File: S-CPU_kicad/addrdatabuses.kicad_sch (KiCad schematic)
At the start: 179 parts

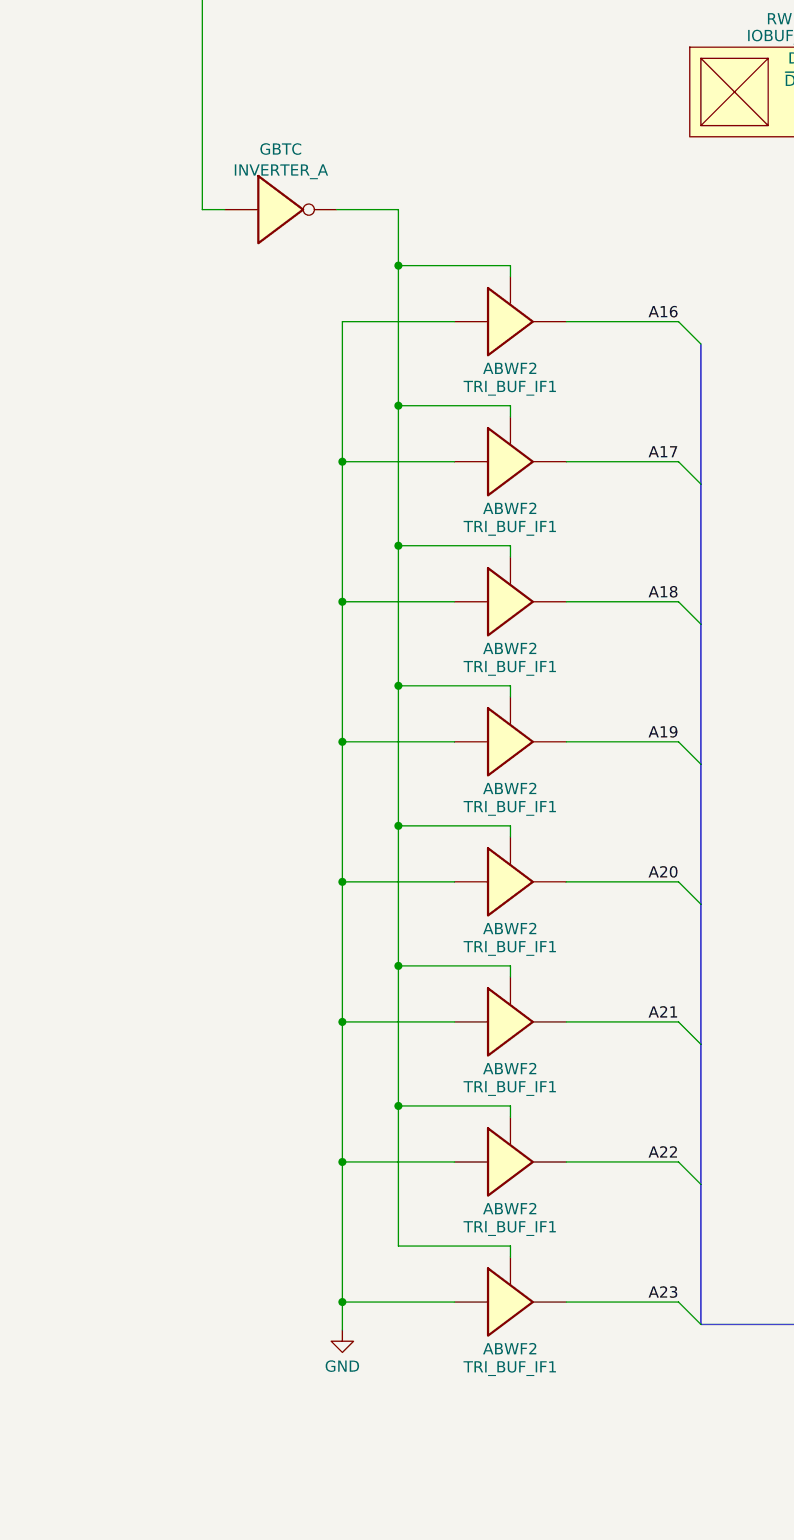
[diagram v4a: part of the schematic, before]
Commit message: Some cells had the wrong ID in the producter remainder sheet. Allocation of new names in spreadsheet for cells in the DMA section
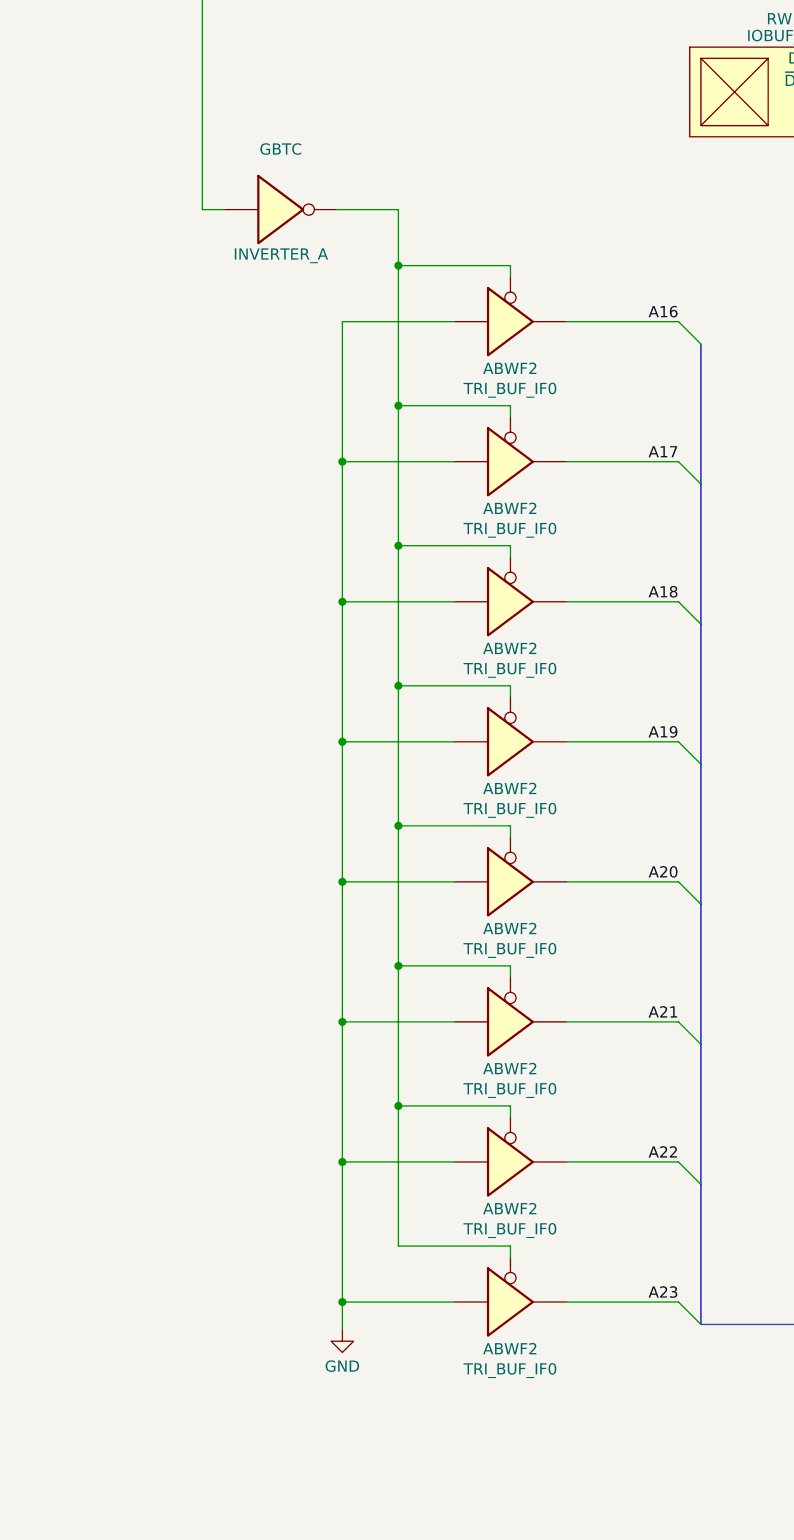
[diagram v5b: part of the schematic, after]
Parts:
- ABWF2: value TRI_BUF_IF1 -> TRI_BUF_IF0; symbol Ricoh_Cells:TRI_BUF_IF1 -> Ricoh_Cells:TRI_BUF_IF0
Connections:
- net A16: now also ABWF2.4; no longer ABWF2.4
- net A17: now also ABWF2.4; no longer ABWF2.4
- net A18: now also ABWF2.4; no longer ABWF2.4
- net A19: now also ABWF2.4; no longer ABWF2.4
- net A20: now also ABWF2.4; no longer ABWF2.4
- net A21: now also ABWF2.4; no longer ABWF2.4
- net A22: now also ABWF2.4; no longer ABWF2.4
- net A23: now also ABWF2.4; no longer ABWF2.4
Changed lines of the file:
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@@
     )
   )
-  (symbol (lib_id "Ricoh_Cells:TRI_BUF_IF1") (at 103.505 212.725 0) (unit 1)
+  (symbol (lib_id "Ricoh_Cells:TRI_BUF_IF0") (at 103.505 133.35 0) (unit 1)
     (in_bom yes) (on_board yes) (dnp no) (fields_autoplaced)
-    (property "Reference" "ABWF2" (at 103.505 218.067 0)
+    (property "Reference" "ABWF2" (at 103.505 138.692 0)
       (effects (font (size 1.27 1.27)))
     )
-    (property "Value" "TRI_BUF_IF1" (at 103.505 220.115 0)
+    (property "Value" "TRI_BUF_IF0" (at 103.505 140.97 0)
       (effects (font (size 1.27 1.27)))
     )
-    (property "Footprint" "" (at 100.965 212.725 0)
+    (property "Footprint" "" (at 100.965 133.35 0)
       (effects (font (size 1.27 1.27)) hide)
     )
-    (property "Datasheet" "http://iceboy.a-singer.de/doc/dmg_cells.html#tri_inv_if0" (at 104.775 222.885 0)
+    (property "Datasheet" "http://iceboy.a-singer.de/doc/dmg_cells.html#tri_buf_if0" (at 104.775 143.51 0)
       (effects (font (size 1.27 1.27)) hide)
     )
@@
     )
   )
-  (symbol (lib_id "Ricoh_Cells:TRI_BUF_IF1") (at 103.505 133.35 0) (unit 1)
+  (symbol (lib_id "Ricoh_Cells:TRI_BUF_IF0") (at 103.505 212.725 0) (unit 1)
     (in_bom yes) (on_board yes) (dnp no) (fields_autoplaced)
-    (property "Reference" "ABWF2" (at 103.505 138.692 0)
+    (property "Reference" "ABWF2" (at 103.505 218.067 0)
       (effects (font (size 1.27 1.27)))
     )
-    (property "Value" "TRI_BUF_IF1" (at 103.505 140.74 0)
+    (property "Value" "TRI_BUF_IF0" (at 103.505 220.345 0)
       (effects (font (size 1.27 1.27)))
     )
-    (property "Footprint" "" (at 100.965 133.35 0)
+    (property "Footprint" "" (at 100.965 212.725 0)
       (effects (font (size 1.27 1.27)) hide)
     )
-    (property "Datasheet" "http://iceboy.a-singer.de/doc/dmg_cells.html#tri_inv_if0" (at 104.775 143.51 0)
+    (property "Datasheet" "http://iceboy.a-singer.de/doc/dmg_cells.html#tri_buf_if0" (at 104.775 222.885 0)
       (effects (font (size 1.27 1.27)) hide)
     )
@@
     )
   )
-  (symbol (lib_id "Ricoh_Cells:TRI_BUF_IF1") (at 103.505 196.85 0) (unit 1)
+  (symbol (lib_id "Ricoh_Cells:TRI_BUF_IF0") (at 103.505 149.225 0) (unit 1)
     (in_bom yes) (on_board yes) (dnp no) (fields_autoplaced)
-    (property "Reference" "ABWF2" (at 103.505 202.192 0)
+    (property "Reference" "ABWF2" (at 103.505 154.567 0)
       (effects (font (size 1.27 1.27)))
     )
-    (property "Value" "TRI_BUF_IF1" (at 103.505 204.24 0)
+    (property "Value" "TRI_BUF_IF0" (at 103.505 156.845 0)
       (effects (font (size 1.27 1.27)))
     )
-    (property "Footprint" "" (at 100.965 196.85 0)
+    (property "Footprint" "" (at 100.965 149.225 0)
       (effects (font (size 1.27 1.27)) hide)
     )
-    (property "Datasheet" "http://iceboy.a-singer.de/doc/dmg_cells.html#tri_inv_if0" (at 104.775 207.01 0)
+    (property "Datasheet" "http://iceboy.a-singer.de/doc/dmg_cells.html#tri_buf_if0" (at 104.775 159.385 0)
       (effects (font (size 1.27 1.27)) hide)
     )
@@
     )
   )
-  (symbol (lib_id "Ricoh_Cells:TRI_BUF_IF1") (at 103.505 228.6 0) (unit 1)
+  (symbol (lib_id "Ricoh_Cells:TRI_BUF_IF0") (at 103.505 117.475 0) (unit 1)
     (in_bom yes) (on_board yes) (dnp no) (fields_autoplaced)
-    (property "Reference" "ABWF2" (at 103.505 233.942 0)
+    (property "Reference" "ABWF2" (at 103.505 122.817 0)
       (effects (font (size 1.27 1.27)))
     )
-    (property "Value" "TRI_BUF_IF1" (at 103.505 235.99 0)
+    (property "Value" "TRI_BUF_IF0" (at 103.505 125.095 0)
       (effects (font (size 1.27 1.27)))
     )
-    (property "Footprint" "" (at 100.965 228.6 0)
+    (property "Footprint" "" (at 100.965 117.475 0)
       (effects (font (size 1.27 1.27)) hide)
     )
-    (property "Datasheet" "http://iceboy.a-singer.de/doc/dmg_cells.html#tri_inv_if0" (at 104.775 238.76 0)
+    (property "Datasheet" "http://iceboy.a-singer.de/doc/dmg_cells.html#tri_buf_if0" (at 104.775 127.635 0)
       (effects (font (size 1.27 1.27)) hide)
     )
@@
     )
   )
-  (symbol (lib_id "Ricoh_Cells:TRI_BUF_IF1") (at 103.505 180.975 0) (unit 1)
+  (symbol (lib_id "Ricoh_Cells:TRI_BUF_IF0") (at 103.505 165.1 0) (unit 1)
     (in_bom yes) (on_board yes) (dnp no) (fields_autoplaced)
-    (property "Reference" "ABWF2" (at 103.505 186.317 0)
+    (property "Reference" "ABWF2" (at 103.505 170.442 0)
       (effects (font (size 1.27 1.27)))
     )
-    (property "Value" "TRI_BUF_IF1" (at 103.505 188.365 0)
+    (property "Value" "TRI_BUF_IF0" (at 103.505 172.72 0)
       (effects (font (size 1.27 1.27)))
     )
-    (property "Footprint" "" (at 100.965 180.975 0)
+    (property "Footprint" "" (at 100.965 165.1 0)
       (effects (font (size 1.27 1.27)) hide)
     )
-    (property "Datasheet" "http://iceboy.a-singer.de/doc/dmg_cells.html#tri_inv_if0" (at 104.775 191.135 0)
+    (property "Datasheet" "http://iceboy.a-singer.de/doc/dmg_cells.html#tri_buf_if0" (at 104.775 175.26 0)
       (effects (font (size 1.27 1.27)) hide)
     )
@@
     )
   )
-  (symbol (lib_id "Ricoh_Cells:TRI_BUF_IF1") (at 103.505 117.475 0) (unit 1)
+  (symbol (lib_id "Ricoh_Cells:TRI_BUF_IF0") (at 103.505 228.6 0) (unit 1)
     (in_bom yes) (on_board yes) (dnp no) (fields_autoplaced)
-    (property "Reference" "ABWF2" (at 103.505 122.817 0)
+    (property "Reference" "ABWF2" (at 103.505 233.942 0)
       (effects (font (size 1.27 1.27)))
     )
-    (property "Value" "TRI_BUF_IF1" (at 103.505 124.865 0)
+    (property "Value" "TRI_BUF_IF0" (at 103.505 236.22 0)
       (effects (font (size 1.27 1.27)))
     )
-    (property "Footprint" "" (at 100.965 117.475 0)
+    (property "Footprint" "" (at 100.965 228.6 0)
       (effects (font (size 1.27 1.27)) hide)
     )
-    (property "Datasheet" "http://iceboy.a-singer.de/doc/dmg_cells.html#tri_inv_if0" (at 104.775 127.635 0)
+    (property "Datasheet" "http://iceboy.a-singer.de/doc/dmg_cells.html#tri_buf_if0" (at 104.775 238.76 0)
       (effects (font (size 1.27 1.27)) hide)
     )
@@
     )
   )
-  (symbol (lib_id "Ricoh_Cells:TRI_BUF_IF1") (at 103.505 165.1 0) (unit 1)
+  (symbol (lib_id "Ricoh_Cells:TRI_BUF_IF0") (at 103.505 180.975 0) (unit 1)
     (in_bom yes) (on_board yes) (dnp no) (fields_autoplaced)
-    (property "Reference" "ABWF2" (at 103.505 170.442 0)
+    (property "Reference" "ABWF2" (at 103.505 186.317 0)
       (effects (font (size 1.27 1.27)))
     )
-    (property "Value" "TRI_BUF_IF1" (at 103.505 172.49 0)
+    (property "Value" "TRI_BUF_IF0" (at 103.505 188.595 0)
       (effects (font (size 1.27 1.27)))
     )
-    (property "Footprint" "" (at 100.965 165.1 0)
+    (property "Footprint" "" (at 100.965 180.975 0)
       (effects (font (size 1.27 1.27)) hide)
     )
-    (property "Datasheet" "http://iceboy.a-singer.de/doc/dmg_cells.html#tri_inv_if0" (at 104.775 175.26 0)
+    (property "Datasheet" "http://iceboy.a-singer.de/doc/dmg_cells.html#tri_buf_if0" (at 104.775 191.135 0)
       (effects (font (size 1.27 1.27)) hide)
     )
@@
     )
   )
-  (symbol (lib_id "Ricoh_Cells:TRI_BUF_IF1") (at 103.505 149.225 0) (unit 1)
+  (symbol (lib_id "Ricoh_Cells:TRI_BUF_IF0") (at 103.505 196.85 0) (unit 1)
     (in_bom yes) (on_board yes) (dnp no) (fields_autoplaced)
-    (property "Reference" "ABWF2" (at 103.505 154.567 0)
+    (property "Reference" "ABWF2" (at 103.505 202.192 0)
       (effects (font (size 1.27 1.27)))
     )
-    (property "Value" "TRI_BUF_IF1" (at 103.505 156.615 0)
+    (property "Value" "TRI_BUF_IF0" (at 103.505 204.47 0)
       (effects (font (size 1.27 1.27)))
     )
-    (property "Footprint" "" (at 100.965 149.225 0)
+    (property "Footprint" "" (at 100.965 196.85 0)
       (effects (font (size 1.27 1.27)) hide)
     )
-    (property "Datasheet" "http://iceboy.a-singer.de/doc/dmg_cells.html#tri_inv_if0" (at 104.775 159.385 0)
+    (property "Datasheet" "http://iceboy.a-singer.de/doc/dmg_cells.html#tri_buf_if0" (at 104.775 207.01 0)
       (effects (font (size 1.27 1.27)) hide)
     )
@@
       (effects (font (size 1.27 1.27)))
     )
-    (property "Value" "INVERTER_A" (at 77.47 100.33 0)
+    (property "Value" "INVERTER_A" (at 77.47 109.855 0)
       (effects (font (size 1.27 1.27)))
     )
@@
         )
         (path "/ca9d3ca9-0297-4b98-a109-b7c162ccc5c3/f34260c0-5998-461e-bddc-407835c1ca78"
-          (reference "GBTC") (unit 1)
+          (reference "GBTD") (unit 1)
         )
       )
